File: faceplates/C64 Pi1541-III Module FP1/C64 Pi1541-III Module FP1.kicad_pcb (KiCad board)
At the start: 2 copper layers, 100 x 35 mm, 9 parts, among them M1 Mounting_Pin, M2 Mounting_Pin, M3 Mounting_Pin, M4 Mounting_Pin

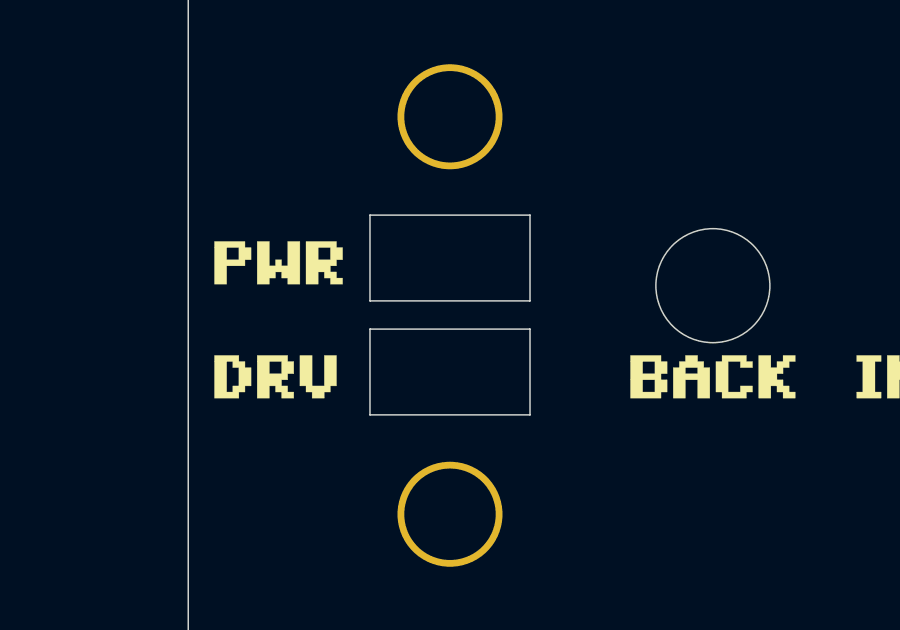
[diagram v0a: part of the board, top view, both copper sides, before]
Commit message: Adjust cutout for LEDs slightly
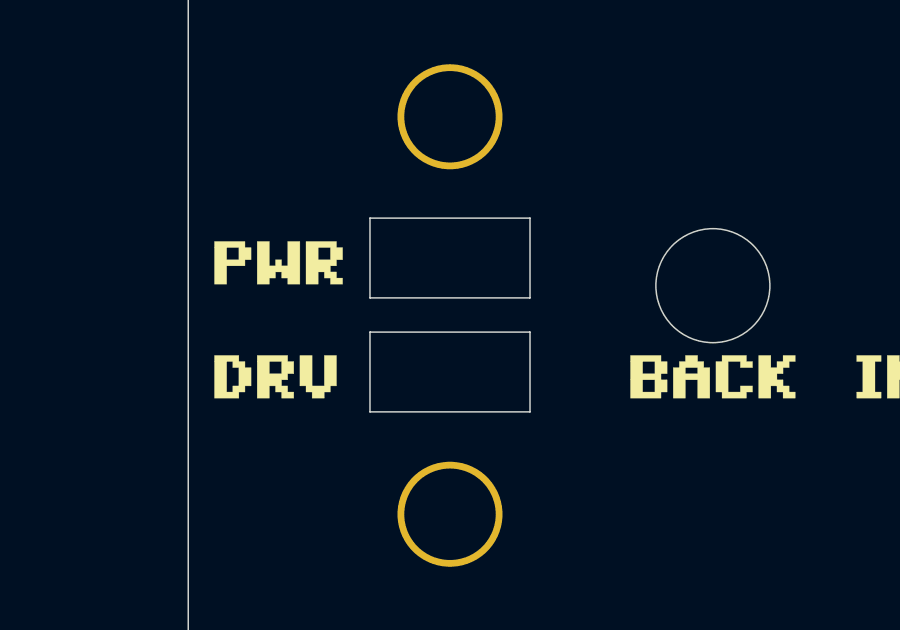
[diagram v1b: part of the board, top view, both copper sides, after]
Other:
- outline, holes or cut-outs redrawn
- board text added: "BulkyMIDI-32 Module FP2 (rev. B) github.com/tebl"
- board text removed: "BulkyMIDI-32 Module FP2 (rev. A) github.com/tebl"
